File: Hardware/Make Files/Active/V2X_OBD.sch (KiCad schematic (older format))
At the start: 92 parts, among them J1 DB9, P20 DB-9 to OBD2, P4 NVM_RST, Q10 2N3904, Q11 2N3904, Q2 2N7002, Q3 3906, Q4 2N3904, Q5 BSS84, Q6 BSS84, Q7 BSS84, Q8 2N3904, Q9 2N7002, SW1 PWR_SW, U11 MCP2551, U5 ESDAxxSC6, U6 ESDAxxSC6, U7 STN1110, U8 LM339, U9 LM317, X2 12M

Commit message: Saving V1.1 as archive.
We are trying a new architecture where the FTDI can be removed. making a
backup spot
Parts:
- removed R16, R19: 10K, Resistors_SMD:R_0603, symbol R
- removed SW1: PWR_SW, Custom Parts:SW-1552.4606, symbol SWITCH_INV
- gave numbers to parts that had none: 2
- renumbered C16 to C30, C17 to C31, C18 to C32, C19 to C33, C20 to C34, C21 to C35, C22 to C36, C23 to C37, C24 to C38, C25 to C39, C41 to C40, C53 to C41, C26 to C42, C27 to C43, D12 to D1, D3 to D2, D4 to D3, D5 to D4, D6 to D5, D13 to D6, P20 to P4, P4 to P5, Q2 to Q1, Q11 to Q10, Q3 to Q2, Q4 to Q3, Q5 to Q4, Q6 to Q5, Q7 to Q6, Q8 to Q7, Q9 to Q8, Q10 to Q9, R7 to R11, R8 to R12, R9 to R13, R10 to R14, R11 to R15, R12 to R16, R13 to R17, R14 to R18, R15 to R19, R17 to R21, R18 to R22, R20 to R23, R21 to R24, R22 to R26, R23 to R27, R24 to R28, R25 to R29, R26 to R30, R27 to R31, R28 to R32, R29 to R33, R6 to R34, R30 to R35, R31 to R36, R32 to R37, R33 to R38, R34 to R39, R35 to R40, R36 to R41, R37 to R42, R40 to R43, R39 to R44, R41 to R46, R42 to R47, R43 to R48, R44 to R49, R45 to R50, R46 to R51, R47 to R52, R48 to R53, R49 to R54, R50 to R55, R51 to R56, U11 to U10
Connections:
- net labels added: 12V0_A, 12V0_B, 3V3_C, 5V0_A, CAN_RXD, CAN_TXD
- net labels removed: 12V0, 12V0RAW, 5V0, PD2, PD3, STN_RXD, STN_TXD
- wire segments 125 -> 122
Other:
- note added: "CAN Terminator"
- note removed: "Automatically Enables CANBUS traciever\nif FTDI contol pins boot to high-z\neasier for initial bring up, simpler fdti setup\nMay reverse for final design, or remove"
- note removed: "Power Switching"
- moved on the sheet: J1, Q4, Q5, Q6, Q9, R35, R36, R37, R40, R41, R42, R43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

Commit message: V1.2 mostly done
BOM is integrated and creates mouser orders
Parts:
- removed C30: 1U, Capacitors_SMD:C_0603, symbol C
- removed C41: 18P, Capacitors_SMD:C_0603, symbol C
- removed C43: 560P, Capacitors_SMD:C_0603, symbol C
- removed D2, D4: RED, LEDs:LED-0805, symbol Led_Small
- removed D3, D5: BLUE, LEDs:LED-0805, symbol Led_Small
- removed D6: 4148, Custom Parts:Diode_0805_12, symbol D
- removed Q1, Q8: 2N7002, Housings_SOT-23_SOT-143_TSOT-6:SOT-23, symbol Q_NMOS_GSD
- removed Q4, Q5: BSS84, Housings_SOT-23_SOT-143_TSOT-6:SOT-23, symbol Q_PMOS_GSD
- removed Q7: 2N3904, Housings_SOT-23_SOT-143_TSOT-6:SOT-23, symbol Q_NPN_BEC
- removed R13, R14, R15: 330, Resistors_SMD:R_0603, symbol R
- removed R24, R31, R35, R49: 10K, Resistors_SMD:R_0603, symbol R
- removed R33: 100K, Resistors_SMD:R_0603, symbol R
- removed R41: 2K2, Resistors_SMD:R_0603, symbol R
- removed R52: 4K7, Resistors_SMD:R_0603, symbol R
- added C44: 560P, Capacitors_SMD:C_0603, symbol C
- added D2: 4148, Custom Parts:Diode_0805_12, symbol D
- added D3, D5: RED, LEDs:LED-0805, symbol LED
- added D4, D6: BLUE, LEDs:LED-0805, symbol LED
- added Q1, Q7: 2N7000, symbol Q_NMOS_SGD
- added Q2, Q3: BSS84, Housings_SOT-23_SOT-143_TSOT-6:SOT-23, symbol Q_PMOS_GSD
- added Q8: 2N3904, Housings_SOT-23_SOT-143_TSOT-6:SOT-23, symbol Q_NPN_BEC
- added R21, R22, R28, R32, R40, R50, R57: 10K, Resistors_SMD:R_0603, symbol R
- added R26: 2K2, Resistors_SMD:R_0603, symbol R
- added R47: 120, Resistors_SMD:R_0603, symbol R
- added R58: 1K, Resistors_SMD:R_0603, symbol R
- C31, C38: value 100N -> 1U; footprint Capacitors_SMD:C_0603 -> (none); Mouse PN (none) -> 603-CC603KRX7R7BB105
- C32: value 4U7 -> 100N; footprint Capacitors_SMD:C_0805 -> Capacitors_SMD:C_0603; Mouse PN (none) -> 810-C1608X7R1E104K
- C33: value 100N -> 4U7; Mouse PN (none) -> 963-LMK212B7475KG-T
- C34, C35: Mouse PN (none) -> 810-C1608X7R1E104K
- C36: value 1U -> 100N; Mouse PN (none) -> 810-C1608X7R1E104K
- C37, C39: footprint Capacitors_SMD:C_0603 -> (none); Mouse PN (none) -> 603-CC603KRX7R7BB105
- C40: value 18P -> 100N; Mouse PN (none) -> 810-C1608X7R1E104K
- C43: renamed from C42; Mouse PN (none) -> 77-VJ0603Y561KXACBC
- D1, D7, D8, D9: Mouse PN (none) -> 821-TS4148-0805-RY
- FB4: Mouse PN (none) -> 810-MPZ1608S221ATA00
- J1: Mouse PN (none) -> 649-D09P13B4PA00LF
- P4: Mouse PN (none) -> NA
- P5: Mouse PN (none) -> 538-22-28-5023
- Q10, Q9: Mouse PN (none) -> 821-MMBT3904
- Q4: renamed from Q6; Mouse PN (none) -> 512-BSS84
- Q5: renamed from Q2; Mouse PN (none) -> 621-MMBT3906-F
- Q6: renamed from Q3; Mouse PN (none) -> 821-MMBT3904
- R15: renamed from R11; Mouse PN (none) -> 71-CRCW0603-62K-E3
- R16: renamed from R12; Mouse PN (none) -> 71-CRCW0603-330-E3
- R17, R18, R19: value 10K -> 330; Mouse PN (none) -> 71-CRCW0603-330-E3
- R20: renamed from R16; Mouse PN (none) -> 71-CRCW0603-10K-E3
- R23: value 2K -> 10K; Mouse PN (none) -> 71-CRCW0603-10K-E3
- R24: renamed from R21; Mouse PN (none) -> 71-CRCW0603-866-E3
- R25: renamed from R22; Mouse PN (none) -> 71-CRCW0603-240-E3
- R27, R29, R39: Mouse PN (none) -> 71-CRCW0603-10K-E3
- R30: value 2K2 -> 10K; Mouse PN (none) -> 71-CRCW0603-10K-E3
- R31: renamed from R26; Mouse PN (none) -> 71-CRCW0603-374-E3
- R33: renamed from R28; value 8K -> 8.87K; Mouse PN (none) -> 71-CRCW0603-8.87K-E3
- R34, R44, R56: value 1K -> 10K; Mouse PN (none) -> 71-CRCW0603-10K-E3
- R35: renamed from R40; Mouse PN (none) -> 71-CRCW0603-2.2K-E3
- R36, R37, R38: value 10K -> 2K2; Mouse PN (none) -> 71-CRCW0603-2.2K-E3
- R41: renamed from R32; Mouse PN (none) -> 71-CRCW0603-1.0K-E3
- R42: value 2K2 -> 100K; Mouse PN (none) -> 71-CRCW0603-100K-E3
- R43, R48: value 10K -> 1K; Mouse PN (none) -> 71-CRCW0603-1.0K-E3
- R45: value 120 -> 10K; Mouse PN (none) -> 71-CRCW0603-10K-E3
- R46: Mouse PN (none) -> 71-CRCW0603-1.0K-E3
- R49: renamed from R47; Mouse PN (none) -> 603-RC1210FR-07510RL
- R51: value 100 -> 10K; Mouse PN (none) -> 71-CRCW0603-10K-E3
- R52: renamed from R50; Mouse PN (none) -> 71-CRCW0603-100-E3
- R53: value 510 -> 100; footprint Resistors_SMD:R_1210 -> Resistors_SMD:R_0603; Mouse PN (none) -> 71-CRCW0603-100-E3
- R54: value 10K -> 4.7K; Mouse PN (none) -> 71-CRCW0603-4.7K-E3
- R55: value 10K -> 510; footprint Resistors_SMD:R_0603 -> Resistors_SMD:R_1210; Mouse PN (none) -> 603-RC1210FR-07510RL
- SW1: Mouse PN (none) -> 653-A6TN-1104
- U10: Mouse PN (none) -> 579-MCP2551-I/SN
- U5, U6: Mouse PN (none) -> 511-ESDA19SC6
- U7: Mouse PN (none) -> SOIC-28
- U8: Mouse PN (none) -> LM339ADR
- U9: Mouse PN (none) -> 863-LM317MSTT3G
- X2: value 12M -> 16MHz; footprint Custom Parts:ABLS7M -> (none); symbol Crystal_Small -> CRYSTAL_SMD; Mouse PN (none) -> 815-AWSCR-16.00MTD-T
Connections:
- wire segments 122 -> 120
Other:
- note added: "16MHz\nOBD Clock"
- note removed: "12MHz OBD Clock"
- moved on the sheet: R16

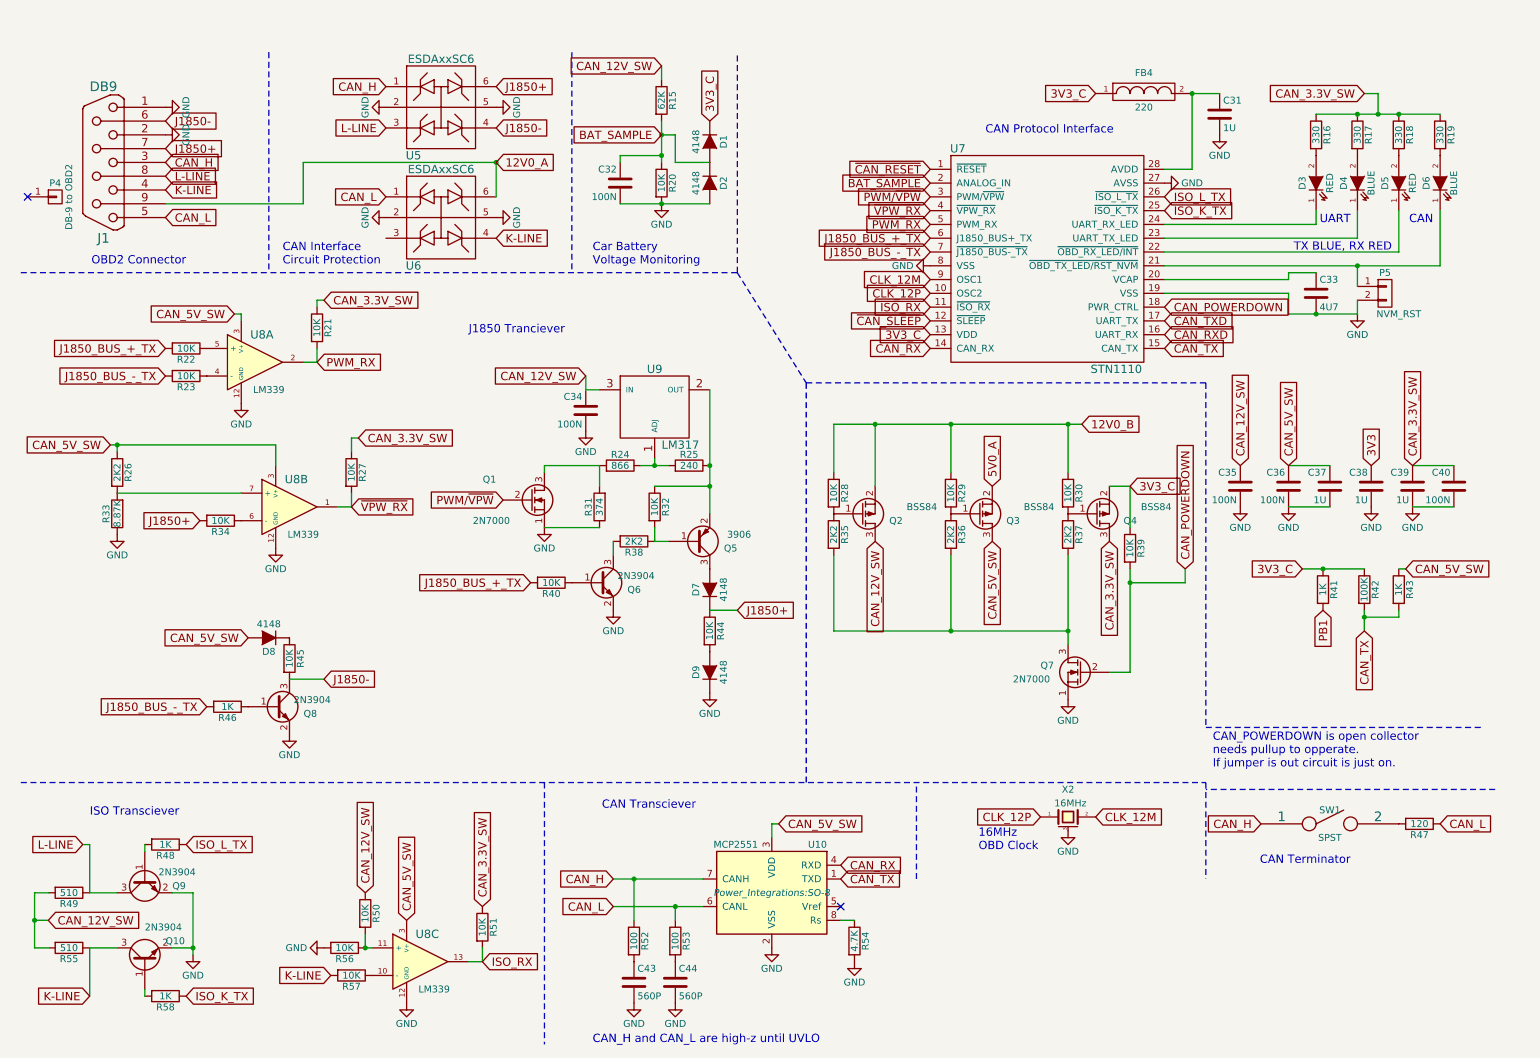
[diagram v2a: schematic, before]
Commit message: V2X v1.2 sch and bom
Made changes to the schematic to V1.2 (remove FTDI possibly) and
integrade the BOM information into the sch
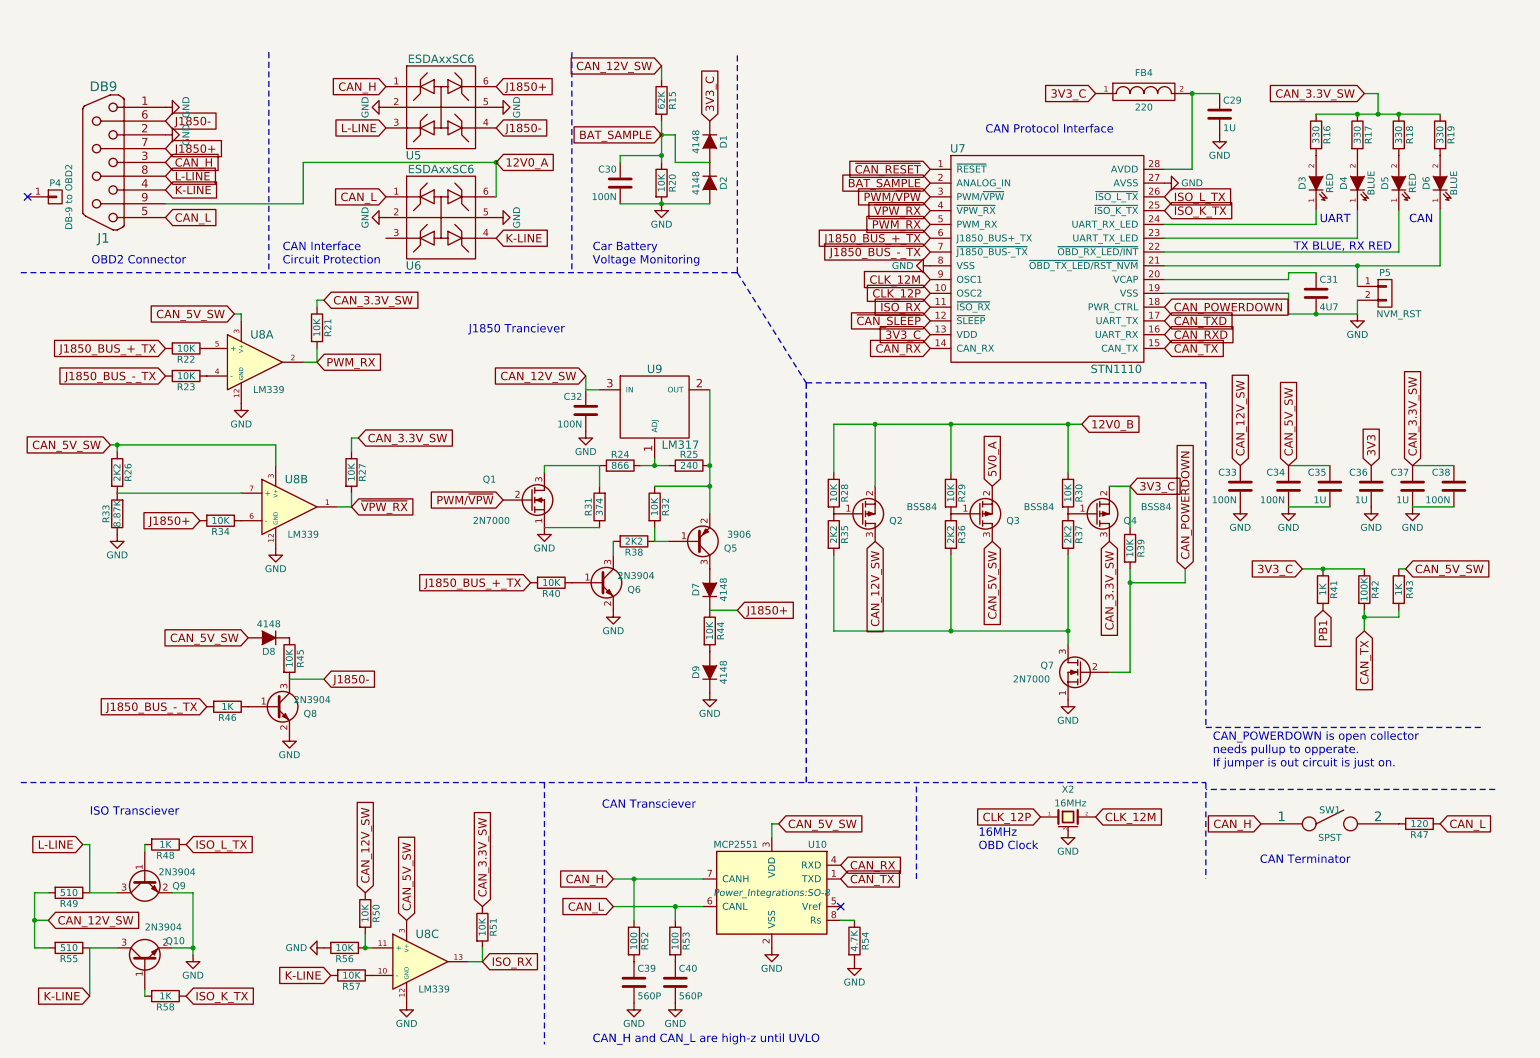
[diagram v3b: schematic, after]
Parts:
- U9: Mouse PN 863-LM317MSTT3G -> 863-LM317MBSTT3G
- renumbered C31 to C29, C32 to C30, C33 to C31, C34 to C32, C35 to C33, C36 to C34, C37 to C35, C38 to C36, C39 to C37, C40 to C38, C43 to C39, C44 to C40

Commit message: Split V2X in 2 boards, layout of SIM pcb done
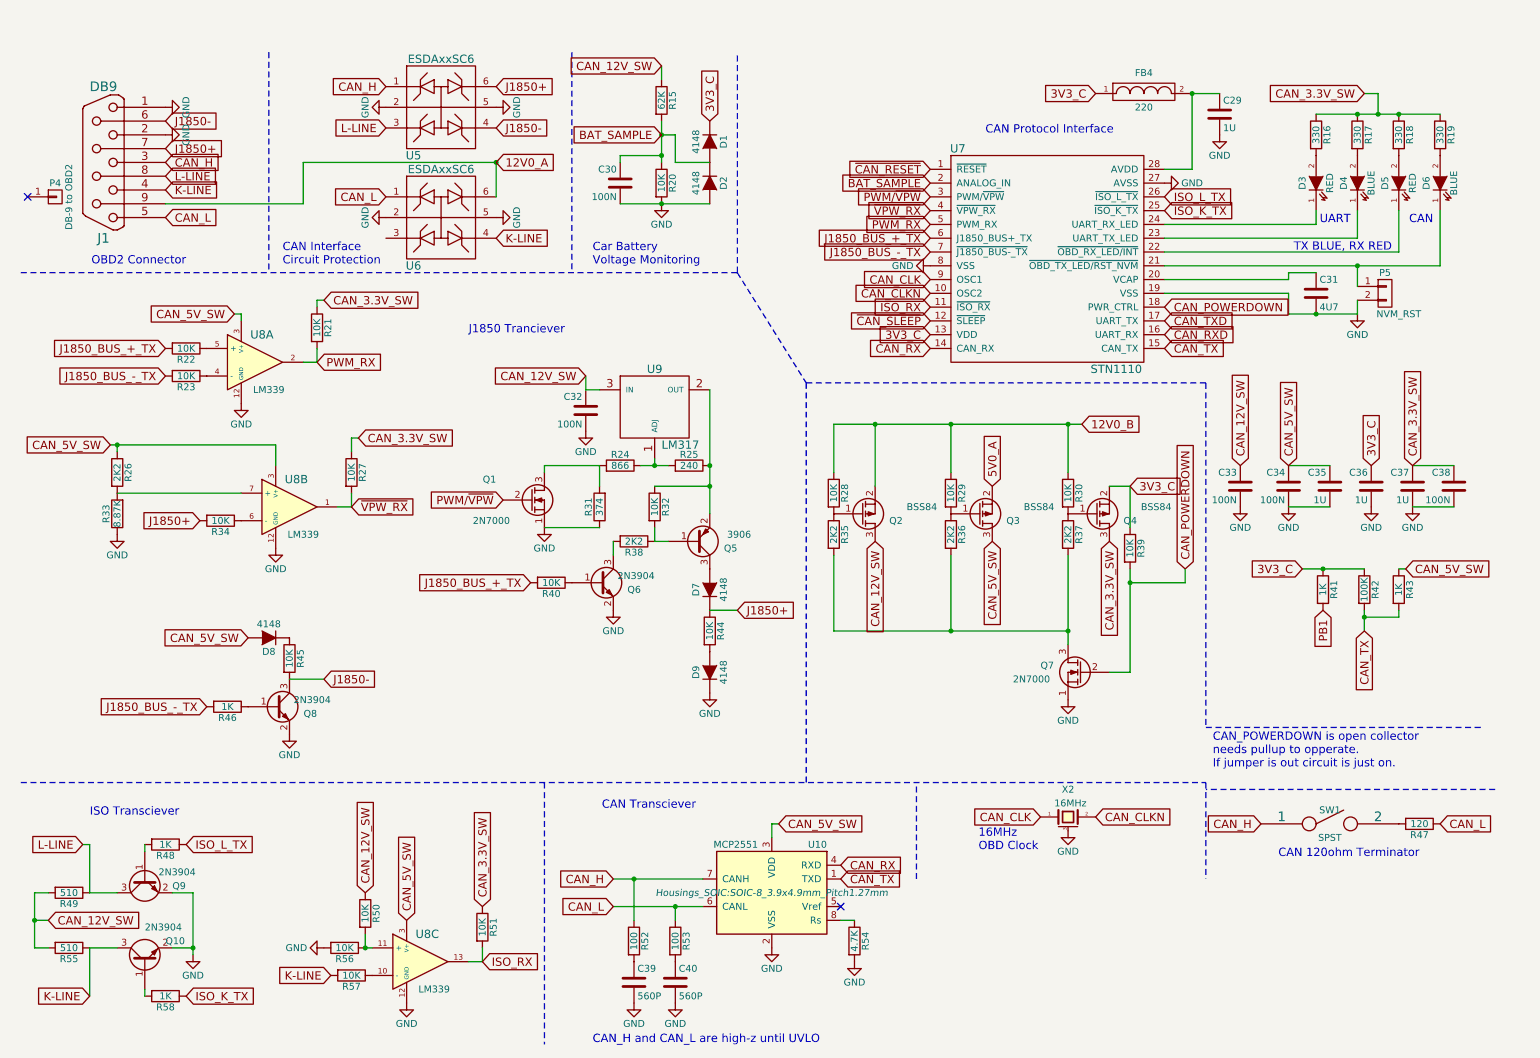
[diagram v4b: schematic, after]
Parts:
- C29, C35, C36, C37: footprint (none) -> Custom Parts:C_0603_SM
- C30, C32, C33, C34, C38, C39, C40: footprint Capacitors_SMD:C_0603 -> Custom Parts:C_0603_SM
- C31: footprint Capacitors_SMD:C_0603 -> Custom Parts:C_0805_SM
- D1, D2, D7, D8, D9: footprint Custom Parts:Diode_0805_12 -> Custom Parts:Diode_0805_12_SM
- FB4: footprint Capacitors_SMD:C_0805 -> Custom Parts:R_0603_sm
- J1: footprint Connect:DB9MC -> Custom Parts:D09P13B4PA00LF
- Q1, Q7: footprint (none) -> Housings_SOT-23_SOT-143_TSOT-6:SOT-23
- R15, R16, R17, R18, R19, R20, R21, R22, R23, R24, R25, R26, R27, R28, R29, R30, R31, R32, R33, R34, R35, R36, R37, R38, R39, R40, R41, R42, R43, R44, R45, R46, R47, R48, R50, R51, R52, R53, R54, R56, R57, R58: footprint Resistors_SMD:R_0603 -> Custom Parts:R_0603_sm
- R49, R55: footprint Resistors_SMD:R_1210 -> Custom Parts:R_1210_SM
- SW1: footprint (none) -> Custom Parts:SW_SPST_A6TN_TH
- U10: footprint Power_Integrations:SO-8 -> Housings_SOIC:SOIC-8_3.9x4.9mm_Pitch1.27mm
- U9: footprint SMD_Packages:SOT-223 -> TO_SOT_Packages_SMD:SOT-223
- X2: footprint (none) -> Custom Parts:AWSCR
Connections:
- net 3V3 is gone; now on net 3V3_C: C36.1
- net CLK_12M renamed CAN_CLK
- net CAN_CLK: now also X2.1; no longer X2.2
- net CLK_12P renamed CAN_CLKN
- net CAN_CLKN: now also X2.2; no longer X2.1
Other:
- note added: "CAN 120ohm Terminator"
- note removed: "CAN Terminator"
